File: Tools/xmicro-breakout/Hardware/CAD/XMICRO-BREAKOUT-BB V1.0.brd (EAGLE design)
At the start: 50.8 x 15.2 mm, 3 parts, among them J1 HDR-17X2

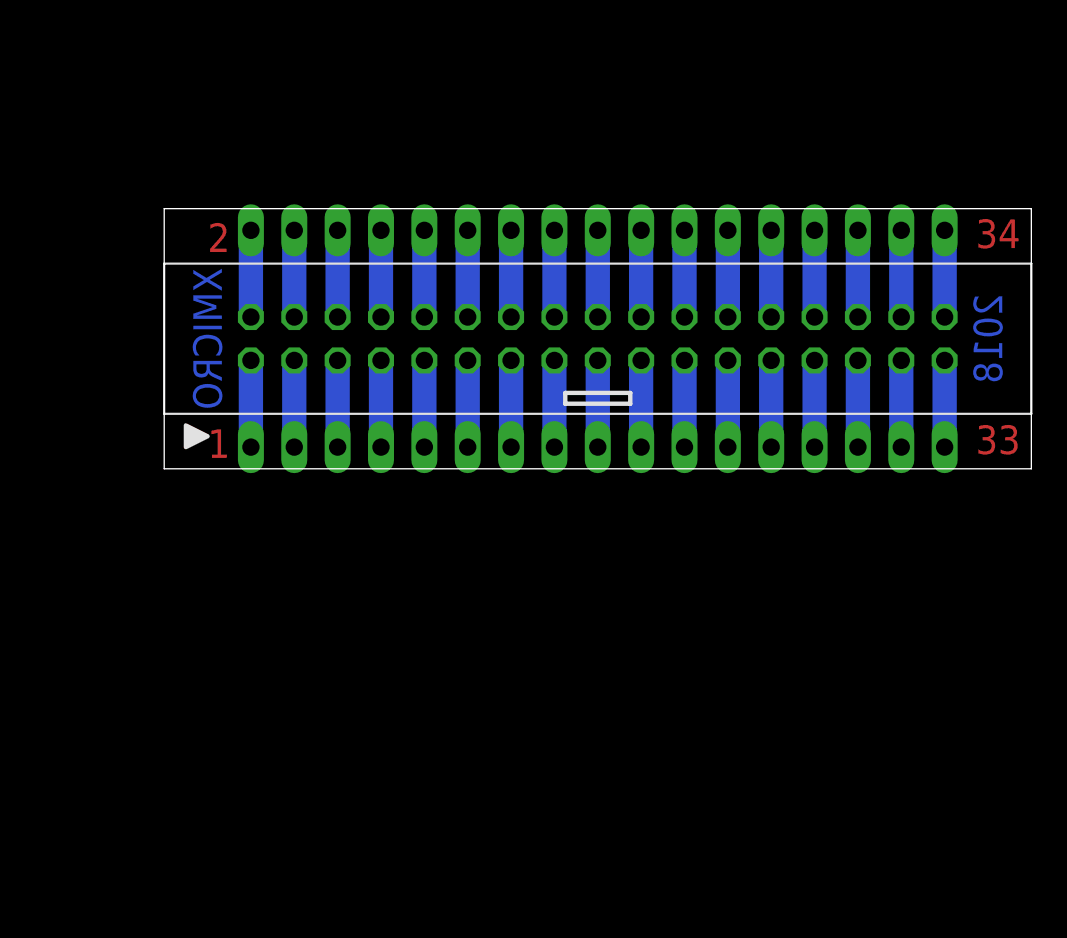
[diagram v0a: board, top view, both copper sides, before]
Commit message: Updated hardware tools to Gen 2
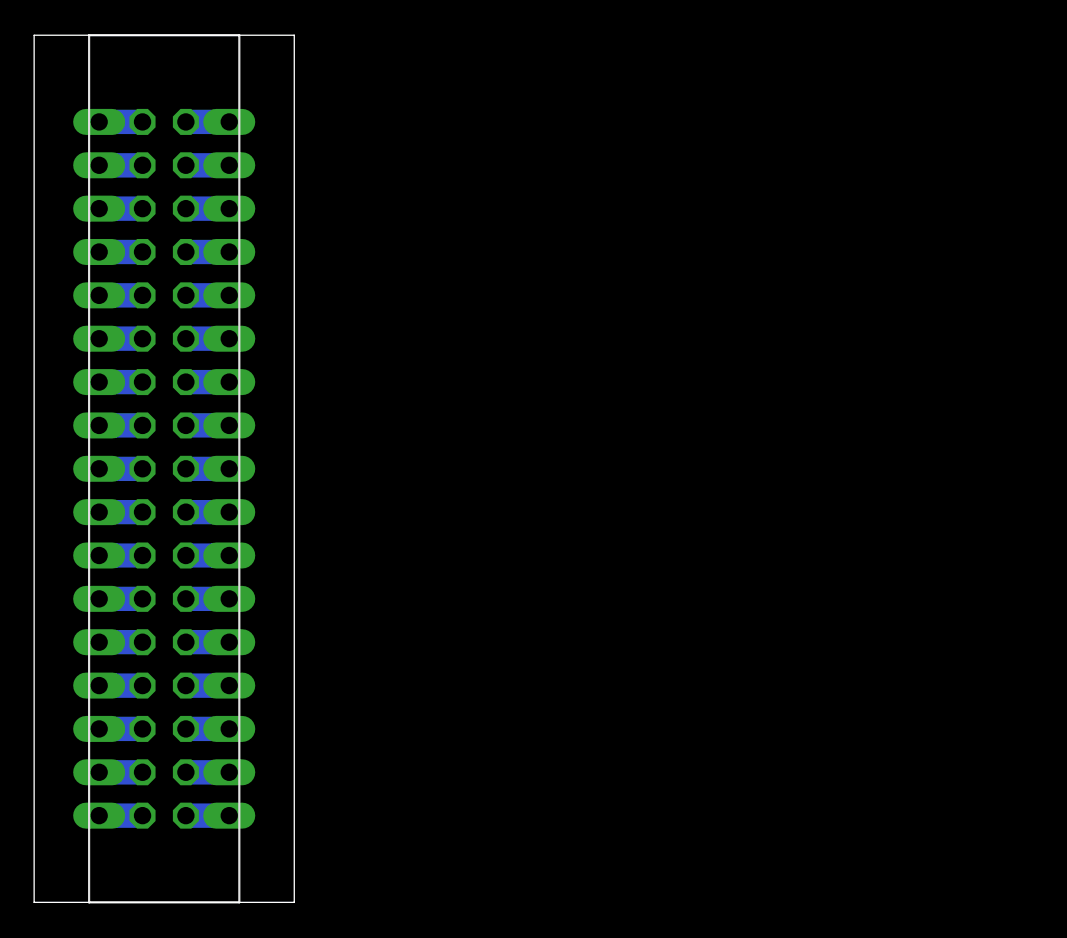
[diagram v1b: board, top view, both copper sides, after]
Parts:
- moved JP1 29.2 mm to (-3.81, 0.00), turned to 270 degrees
- moved J1 26.5 mm to (0.00, 0.00), turned to 270 degrees
- moved JP2 25.7 mm to (3.81, 0.00), turned to 270 degrees
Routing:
- net N$9: track 5.08 -> 2.54 mm
- net N$8: track 5.08 -> 2.54 mm
- net N$7: track 5.08 -> 2.54 mm
- net N$6: track 5.08 -> 2.54 mm
- net N$5: track 5.08 -> 2.54 mm
- net N$4: track 5.08 -> 2.54 mm
- net N$35: track 5.08 -> 2.54 mm
- net N$34: track 5.08 -> 2.54 mm
- net N$33: track 5.08 -> 2.54 mm
- net N$32: track 5.08 -> 2.54 mm
- net N$31: track 5.08 -> 2.54 mm
- net N$30: track 5.08 -> 2.54 mm
- net N$3: track 5.08 -> 2.54 mm
- net N$29: track 5.08 -> 2.54 mm
- net N$28: track 5.08 -> 2.54 mm
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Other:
- board size 50.8 x 15.2 mm -> 15.2 x 50.8 mm
- board text added: "!BAK"
- board text added: "!BRQ"
- board text added: "!CSX"
- board text added: "!FET"
- board text added: "!HLT"
- board text added: "!INH"
- board text added: "!IOS"
- board text added: "!IQX"
- board text added: "!NMI"
- board text added: "!RD"
- board text added: "!RST"
- board text added: "!SIN"
- board text added: "!V0"
- board text added: "!V1"
- board text added: "!V2"
- board text added: "!V3"
- board text added: "!V4"
- board text added: "!V5"
- board text added: "!V6"
- board text added: "!V7"
- board text added: "!WAI"
- board text added: "!WR"
- board text added: "+12"
- board text added: "+5V"
- board text added: "-12"
- board text added: "0V"
- board text added: "3V3"
- board text added: "5SB"
- board text added: "A0"
- board text added: "A1"
- board text added: "A10"
- board text added: "A11"
- board text added: "A12"
- board text added: "A13"
- board text added: "A14"
- board text added: "A15"
- board text added: "A16"
- board text added: "A17"
- board text added: "A18"
- board text added: "A19"
- board text added: "A2"
- board text added: "A3"
- board text added: "A4"
- board text added: "A5"
- board text added: "A6"
- board text added: "A7"
- board text added: "A8"
- board text added: "A9"
- board text added: "CLK"
- board text added: "D0"
- board text added: "D1"
- board text added: "D2"
- board text added: "D3"
- board text added: "D4"
- board text added: "D5"
- board text added: "D6"
- board text added: "D7"
- board text removed: "1"
- board text removed: "2"
- board text removed: "2018"
- board text removed: "33"
- board text removed: "34"
- board text removed: "XMICRO"
